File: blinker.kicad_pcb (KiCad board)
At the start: 2 copper layers, 28 parts, among them J1 TEST_1P, J2 TEST_1P, J3 TEST_1P, J4 TEST_1P, J5 TEST_1P, J6 TEST_1P, J7 TEST_1P, J8 TEST_1P, J9 TOUCH_PAD_COPPER, Q1 NTR4003NT3G, Q2 NTR4003NT3G, Q3 NTR4003NT3G, Q4 NTR4003NT3G, U1 ASMB-MTB0-0A3A2, U2 ASMB-MTB0-0A3A2, U3 ATTINY85V-10SU

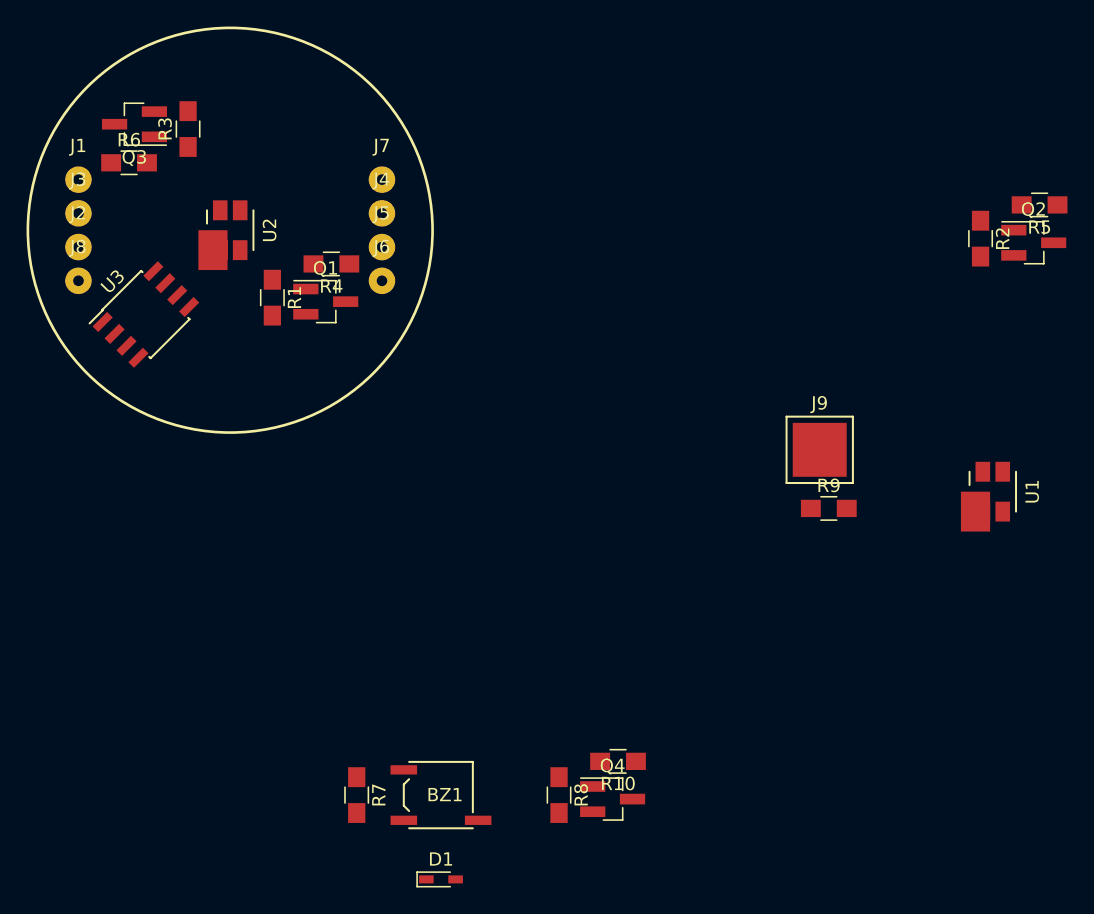
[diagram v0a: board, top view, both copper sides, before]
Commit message: decouplign cap and pullup on reset, plus routing almost done
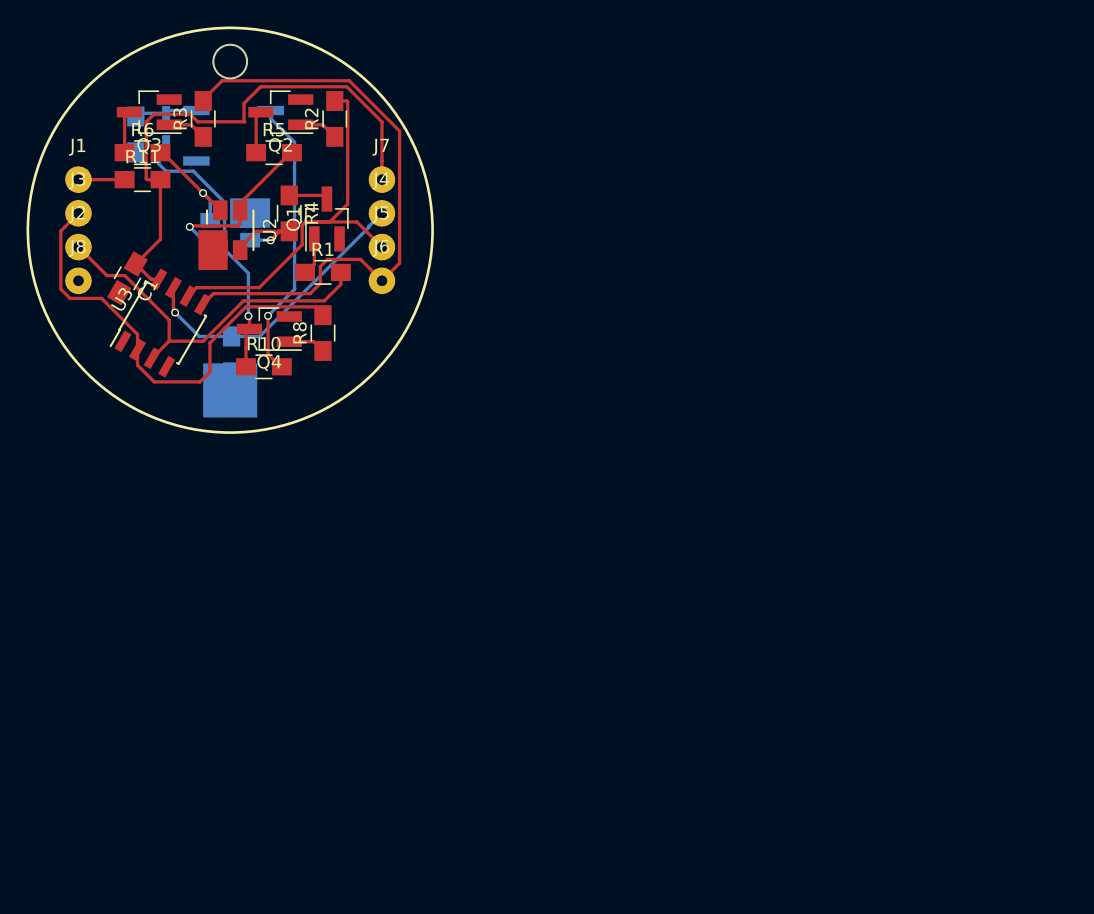
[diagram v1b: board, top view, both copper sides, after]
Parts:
- added C1: 100nf, Capacitors_SMD:C_0805_HandSoldering, F.Cu at (112.9, 86.2)
- added R11: 20K, Resistors_SMD:R_0805_HandSoldering, F.Cu at (114.0, 78.7)
- BZ1, D1, J9, R7, R9, U1: moved to B.Cu
- moved U1 60.7 mm to (120.7, 82.5), turned to 270 degrees
- moved D1 60.3 mm to (115.8, 74.8), turned to 270 degrees
- moved R5 57.8 mm to (124.0, 76.7), turned to 0 degrees
- moved Q2 57.6 mm to (124.5, 73.7), turned to 180 degrees
- moved R7 52.5 mm to (113.5, 75.3), turned to 90 degrees
- moved BZ1 52.1 mm to (120.9, 75.4)
- moved R2 49.5 mm to (128.5, 74.2), turned to 90 degrees
- moved R9 46.5 mm to (120.8, 91.9), turned to 270 degrees
- moved J9 44.6 mm to (120.7, 94.6)
- moved Q4 43.8 mm to (123.6, 90.0), turned to 180 degrees
- moved R10 39.9 mm to (123.2, 92.8), turned to 0 degrees
- moved R8 39.1 mm to (127.6, 90.3), turned to 90 degrees
- moved Q1 6.23 mm to (127.9, 81.7), turned to 90 degrees
- moved R4 4.96 mm to (125.1, 81.3), turned to 270 degrees
- moved R1 4.26 mm to (127.6, 85.7), turned to 0 degrees
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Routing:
- net /BLUE: track 0.00 -> 45.2 mm
- net VCC: track 0.00 -> 40.4 mm
- net /BUZZER: track 0.00 -> 34.2 mm
- net /GREEN: track 0.00 -> 30.6 mm
- net /RED: track 0.00 -> 28.1 mm
- net /TOUCH: track 0.00 -> 22.1 mm, vias 0 -> 1
- net Net-(BZ1-Pad2): track 0.00 -> 21.5 mm, vias 0 -> 1
- net Net-(D1-Pad2): track 0.00 -> 21.4 mm, vias 0 -> 1
- net /GREEN_MOS: track 0.00 -> 12.9 mm, vias 0 -> 1
- net /BLUE_MOS: track 0.00 -> 8.57 mm, vias 0 -> 1
- net /RED_MOS: track 0.00 -> 7.63 mm, vias 0 -> 1
- net Net-(BZ1-Pad1): track 0.00 -> 4.75 mm
- net /RESET: track 0.00 -> 3.48 mm
- net Net-(Q3-Pad3): track 0.00 -> 3.20 mm
- net Net-(Q2-Pad3): track 0.00 -> 3.20 mm
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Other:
- board outline added: 2.5 x 2.5 mm

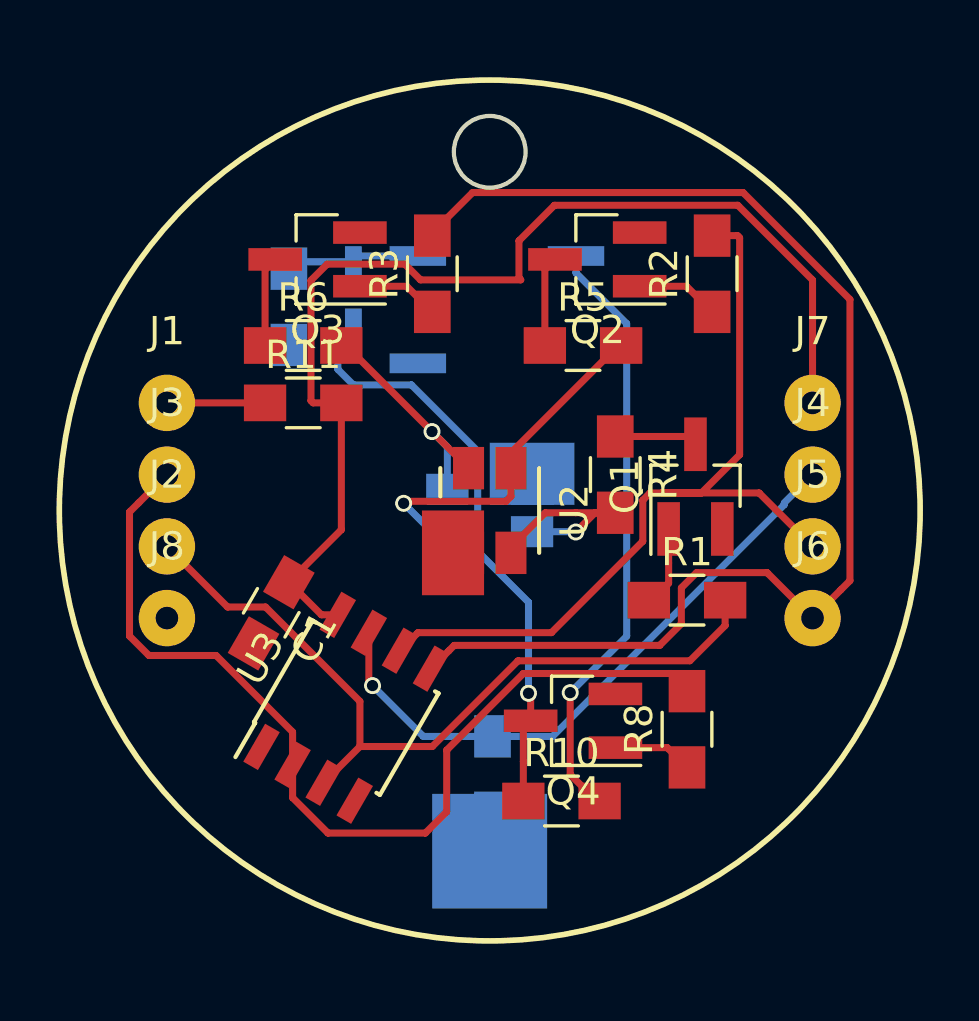
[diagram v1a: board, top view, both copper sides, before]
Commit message: pdc not in sync with sch, but silk almost done
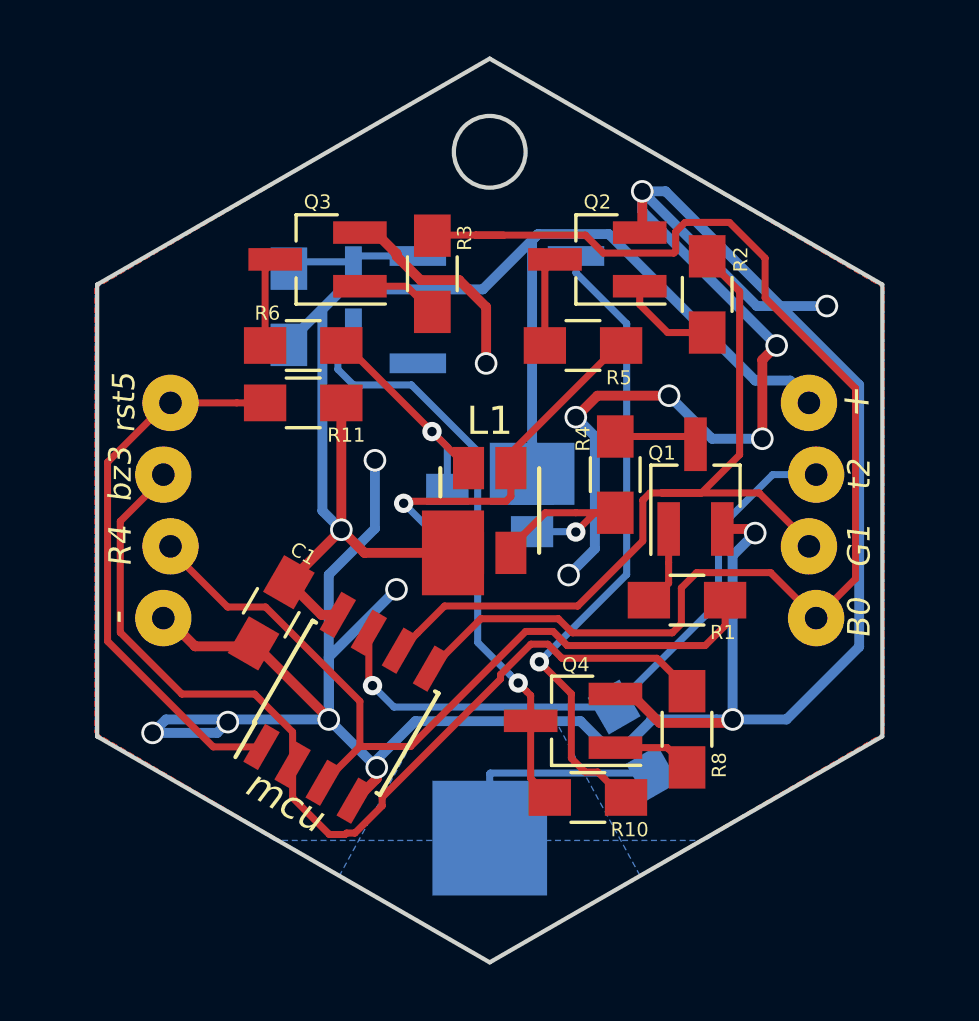
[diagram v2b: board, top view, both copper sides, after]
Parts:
- removed U1, U2: ASMB-MTB0-0A3A2, ASMB-MTB0-0A3A2:ASMB-MTB0-0A3A2
- added L1: ASMB-MTB0-0A3A2, ASMB-MTB0-0A3A2:ASMB-MTB0-0A3A2, F.Cu at (120.7, 82.5)
- added L2: ASMB-MTB0-0A3A2, ASMB-MTB0-0A3A2:ASMB-MTB0-0A3A2, B.Cu at (120.7, 82.5)
- moved R9 5.13 mm to (125.7, 90.7), turned to 300 degrees
- moved R10 0.94 mm to (124.1, 92.7)
- moved R2 0.75 mm to (128.3, 74.9)
- moved click 0.46 mm to (120.7, 94.2)
- moved + 0.13 mm to (132.0, 78.7)
- moved G1 0.13 mm to (132.0, 83.8)
- moved - 0.13 mm to (109.1, 86.4)
- moved R4 0.13 mm to (109.3, 83.8)
- moved bz3 0.13 mm to (109.1, 81.3)
- moved rst5 0.13 mm to (109.3, 78.7)
- moved B0 0.13 mm to (132.2, 86.4)
- moved t2 0.13 mm to (132.2, 81.3)
- renumbered J7 to +, J8 to -, J6 to B0, J5 to G1, J2 to R4, J3 to bz3, J9 to click, U3 to mcu, J1 to rst5, J4 to t2
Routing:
- net GND: track 0.00 -> 130.4 mm, vias 0 -> 16
- net /RESET: track 3.48 -> 19.8 mm
- net VCC: track 40.4 -> 54.0 mm, vias 0 -> 1
- net Net-(J9-Pad1): track 0.00 -> 8.05 mm
- net Net-(BZ1-Pad2): track 21.5 -> 22.8 mm
- net /GREEN: track 30.6 -> 29.5 mm
- net /TOUCH: track 22.1 -> 22.9 mm
- net /BLUE: track 45.2 -> 46.0 mm
- net Net-(Q2-Pad1): track 2.94 -> 3.50 mm
- added copper zone on F.Cu, net (none)
- added copper zone on B.Cu, net GND
- added copper zone on F.Cu, net GND
- added copper zone on B.Cu, net Net-(J9-Pad1)
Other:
- board size 2.5 x 2.5 mm -> 27.8 x 32 mm
- net class Default: clearance 0.2 -> 0.1524; trace_width 0.25 -> 0.1524; via_dia 0.6 -> 0.6858; via_drill 0.4 -> 0.3302
- net class pwr added: clearance 0.1524, trace_width 0.3048, via_dia 0.8128, via_drill 0.6096
- rule trace_clearance: 0.2 -> 0.1524
- rule trace_min: 0.2 -> 0.1524
- rule via_min_drill: 0.3 -> 0.3302
- rule via_min_size: 0.4 -> 0.6858
- board text added: "+"
- board text added: "-"
- board text added: "B0"
- board text added: "G1"
- board text added: "R4"
- board text added: "bz3"
- board text added: "rst5"
- board text added: "t2"

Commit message: drill and cosmetic
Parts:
- added G***: LOGO, blinker_attiny85:testfoto, B.Cu at (113.0, 89.2)
- added REF**: MountingHole_2.7mm_M2.5, Mounting_Holes:MountingHole_2.7mm_M2.5, F.Cu at (120.7, 69.8)
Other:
- outline, holes or cut-outs redrawn
- board text added: "Sul on ilus naeratus"

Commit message: 2 version, already built, ready to be tested
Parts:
- removed the + at (132.0, 78.7)
- removed the - at (109.1, 86.4)
- removed the R4 at (109.3, 83.8)
- removed the R4 at (125.1, 81.3)
- removed the REF** at (120.7, 69.8)
- removed click: TOUCH_PAD_COPPER, SMD_Packages:1Pin
- removed mcu: ATTINY85V-10SU, Housings_SOIC:SOIC-8_3.9x4.9mm_Pitch1.27mm
- added +: TEST_1P, Wire_Pads:SolderWirePad_single_1-2mmDrill, F.Cu at (12.6, -3.81)
- added +: TEST_1P, wrirepad:singlesolderpad, B.Cu at (5.08, -10.2)
- added -: TEST_1P, Wire_Pads:SolderWirePad_single_1-2mmDrill, F.Cu at (-12.8, 3.81)
- added -: TEST_1P, wrirepad:singlesolderpad, B.Cu at (-5.08, -10.2)
- added G***: LOGO, blinker_attiny85:italia, B.Cu at (-11.0, 7.00)
- added J9: TOUCH_PAD_COPPER, SMD_Packages:1Pin, B.Cu at (0.00, 11.4)
- added R4: 33R, Resistors_SMD:R_0805, F.Cu at (5.08, -1.91)
- added R4: TEST_1P, Wire_Pads:SolderWirePad_single_1-2mmDrill, F.Cu at (-12.6, 1.27)
- added REF**: SolderWirePad_single_2mmDrill, Wire_Pads:SolderWirePad_single_2mmDrill, F.Cu at (0.00, -12.8)
- added mcu1: ATTINY85V-10SU, Housings_SOIC:SOIJ-8_5.3x5.3mm_Pitch1.27mm, F.Cu at (-5.08, 7.62)
- B0, G1, bz3, rst5, t2: footprint Wire_Pads:SolderWirePad_single_0-8mmDrill -> Wire_Pads:SolderWirePad_single_1-2mmDrill
- C1: footprint Capacitors_SMD:C_0805_HandSoldering -> Capacitors_SMD:C_0805
- G***: moved to F.Cu
- Q1, Q2, Q3: footprint TO_SOT_Packages_SMD:SOT-23_Handsoldering -> TO_SOT_Packages_SMD:SOT-23
- Q4: footprint TO_SOT_Packages_SMD:SOT-23_Handsoldering -> TO_SOT_Packages_SMD:SOT-23; moved to B.Cu
- R1, R11, R2, R3, R7: footprint Resistors_SMD:R_0805_HandSoldering -> Resistors_SMD:R_0805
- R10: value 27R -> 33R; footprint Resistors_SMD:R_0805_HandSoldering -> Resistors_SMD:R_0805; moved to B.Cu
- R5, R6: value 34R -> 33R; footprint Resistors_SMD:R_0805_HandSoldering -> Resistors_SMD:R_0805
- R8: footprint Resistors_SMD:R_0805_HandSoldering -> Resistors_SMD:R_0805; moved to B.Cu
- R9: value 10K -> 20K; footprint Resistors_SMD:R_0805_HandSoldering -> Resistors_SMD:R_0805
- moved R10 161.0 mm to (-5.71, -2.54), turned to 90 degrees
- moved R2 155.3 mm to (-3.17, -7.62), turned to 270 degrees
- moved R9 151.6 mm to (0.00, 6.05), turned to 270 degrees
- moved Q1 150.4 mm to (5.08, -5.08), turned to 180 degrees
- moved R1 150.0 mm to (8.26, -5.08), turned to 90 degrees
- moved Q2 148.6 mm to (0.00, -7.62), turned to 0 degrees
- moved R5 148.2 mm to (0.00, -4.45)
- moved bz3 147.2 mm to (-12.8, -1.27), turned to 270 degrees
- moved rst5 147.2 mm to (-12.6, -3.81), turned to 270 degrees
- moved R8 147.0 mm to (6.99, 6.35), turned to 180 degrees
- moved C1 146.7 mm to (-7.62, 2.54), turned to 60 degrees
- moved L1 146.2 mm to (0.00, 0.00)
- moved L2 146.2 mm to (0.00, 0.00), turned to 90 degrees
- moved BZ1 145.6 mm to (0.00, -5.71), turned to 180 degrees
- moved Q4 145.4 mm to (6.99, 3.17), turned to 90 degrees
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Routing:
- net GND: track 130.4 -> 49.9 mm, vias 16 -> 3
- net /BLUE: track 46.0 -> 15.5 mm
- net Net-(BZ1-Pad2): track 22.8 -> 3.05 mm, vias 1 -> 0
- net /GREEN: track 29.5 -> 45.9 mm
- net /RED: track 28.5 -> 39.2 mm
- net VCC: track 54.0 -> 43.4 mm
- net /RED_MOS: track 7.63 -> 16.9 mm
- net /GREEN_MOS: track 12.9 -> 5.59 mm
- net /BUZZER: track 34.5 -> 28.3 mm, vias 0 -> 1
- net Net-(D1-Pad2): track 21.7 -> 16.8 mm, vias 1 -> 0
- net /RESET: track 19.8 -> 15.6 mm, vias 0 -> 1
- net /BLUE_MOS: track 8.57 -> 12.4 mm, vias 1 -> 2
- net Net-(J9-Pad1): track 8.05 -> 4.43 mm
- net /TOUCH: track 22.9 -> 25.8 mm
- net Net-(Q2-Pad1): track 3.50 -> 2.17 mm
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- added copper zone on F.Cu, net Net-(J9-Pad1)
- removed copper zone on F.Cu, net (none)
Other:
- board size 27.8 x 32 mm -> 30.3 x 33.9 mm
- net class 0.2mm added: clearance 0.2, trace_width 0.2, via_dia 0.6858, via_drill 0.3302
- net class Default: clearance 0.1524 -> 0.254; trace_width 0.1524 -> 0.254
- net class Minimal added: clearance 0.1524, trace_width 0.1524, via_dia 0.6858, via_drill 0.3302
- net class pwr removed
- rule pad_to_mask_clearance: 0.2 -> 0.05
- rule trace_clearance: 0.1524 -> 0.254
- board text added: "click"
- board text removed: "+"
- board text removed: "-"
- board text removed: "B0"
- board text removed: "G1"
- board text removed: "R4"
- board text removed: "Sul on ilus naeratus"
- board text removed: "bz3"
- board text removed: "rst5"
- board text removed: "t2"
